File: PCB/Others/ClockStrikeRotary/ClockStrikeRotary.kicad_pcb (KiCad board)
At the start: 2 copper layers, 98 x 52 mm, 25 parts, among them J1 In, J2 Out, J3 Port 1, J4 Port 2, SW1 Rotary_Encoder_Switch

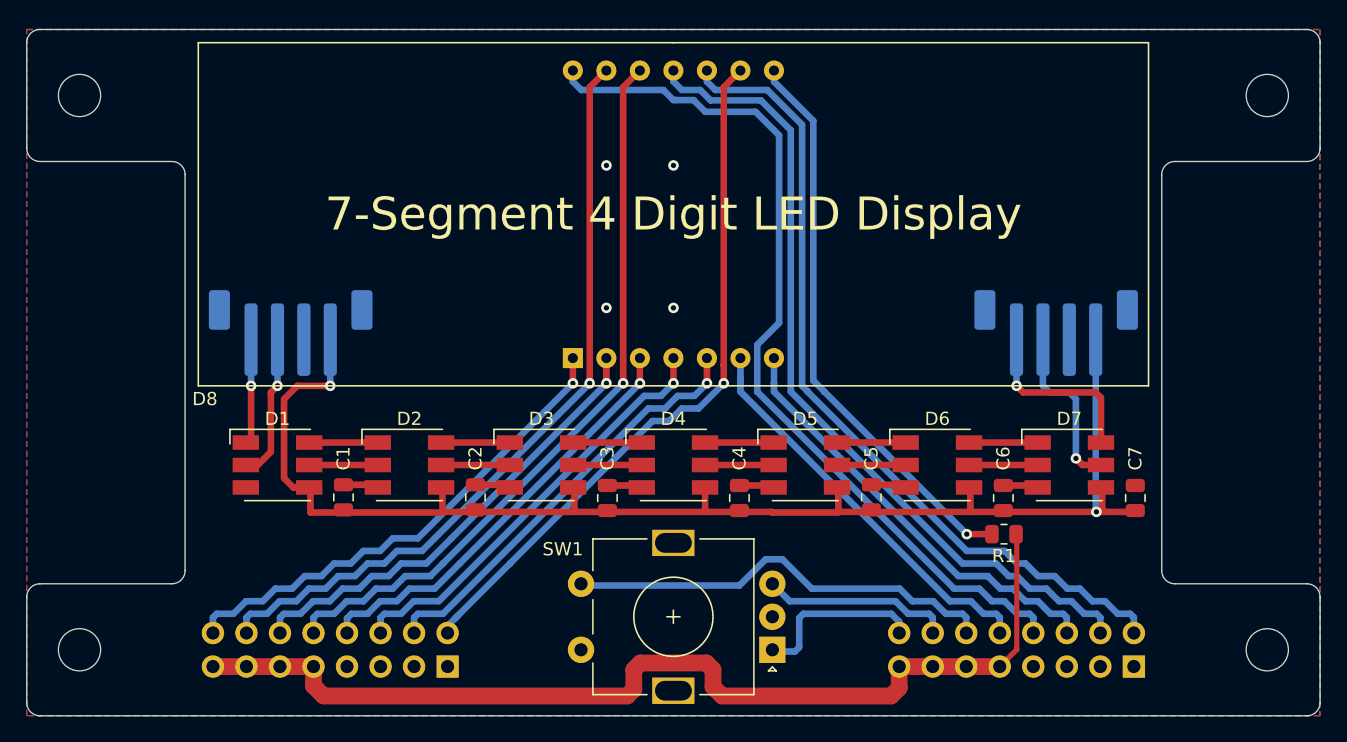
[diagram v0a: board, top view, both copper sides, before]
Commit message: Convert all KiCad to 6.0, clean up libraries, remove files that shouldn't be committed.
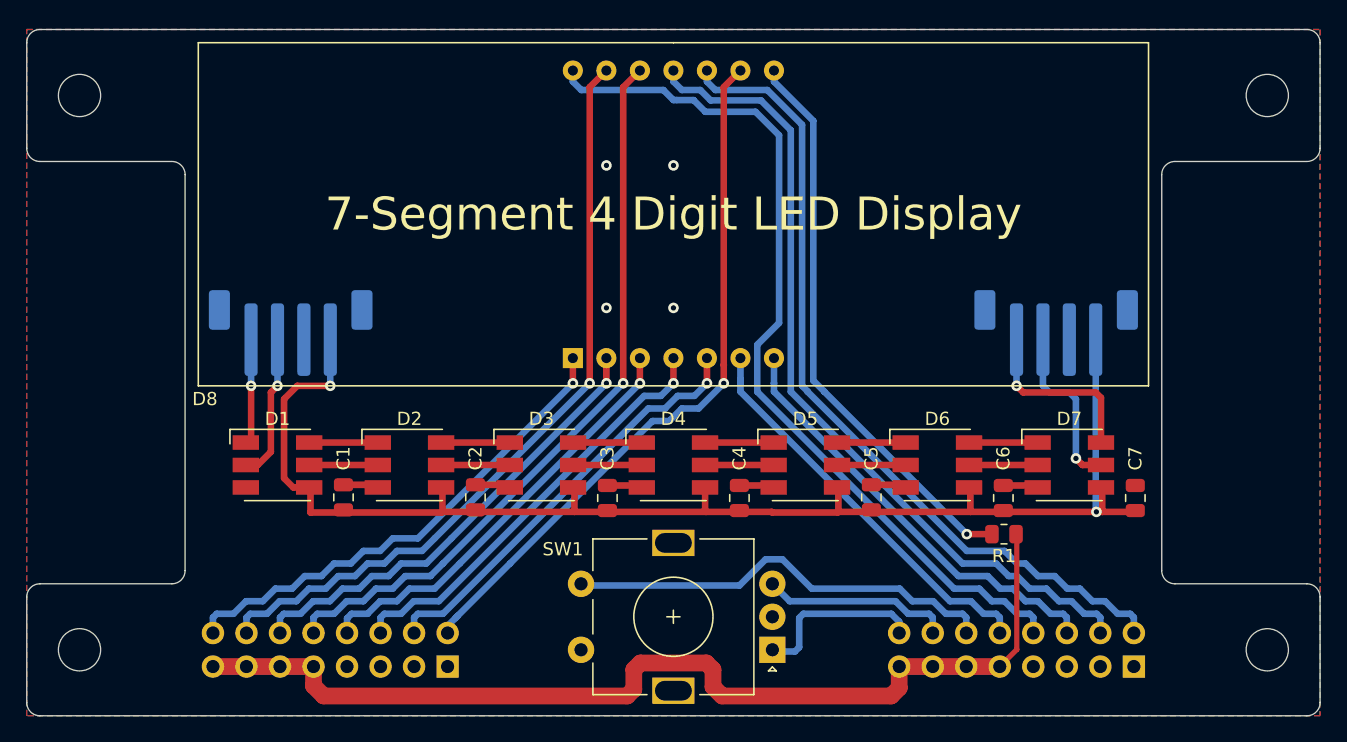
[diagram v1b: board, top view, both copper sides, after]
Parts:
- J3, J4: footprint Custom:PinHeader_2x08_P2.54mm_Vertical-Centered -> KTANE:PinHeader_2x08_P2.54mm_Vertical-Centered
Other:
- net class Default removed

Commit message: First pass of PCB rework.
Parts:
- removed J2: Out, Connector_JST:JST_PH_B4B-PH-SM4-TB_1x04-1MP_P2.00mm_Vertical
- removed REF** (x4): MountingHole_3.2mm_M3, MountingHole:MountingHole_3.2mm_M3
- added C10: 4.7nF, Capacitor_SMD:C_0603_1608Metric, B.Cu at (80.4, 66.3)
- added C11: 10uF, Capacitor_SMD:C_0603_1608Metric, B.Cu at (96.6, 41.2)
- added C12: 0.1μF, Capacitor_SMD:C_0603_1608Metric, B.Cu at (97.4, 38.9)
- added C8: 4.7nF, Capacitor_SMD:C_0603_1608Metric, B.Cu at (86.5, 66.3)
- added C9: 4.7nF, Capacitor_SMD:C_0603_1608Metric, B.Cu at (83.4, 66.3)
- added H1: MountingHole, MountingHole:MountingHole_3.2mm_M3, F.Cu at (20.0, 29.0)
- added H2: MountingHole, MountingHole:MountingHole_3.2mm_M3, F.Cu at (20.0, 71.0)
- added H3: MountingHole, MountingHole:MountingHole_3.2mm_M3, F.Cu at (110.0, 29.0)
- added H4: MountingHole, MountingHole:MountingHole_3.2mm_M3, F.Cu at (110.0, 71.0)
- added Q10: Q_NMOS_GSD, Package_TO_SOT_SMD:SOT-23, B.Cu at (64.5, 30.2)
- added Q11: Q_NMOS_GSD, Package_TO_SOT_SMD:SOT-23, B.Cu at (68.1, 30.2)
- added Q12: Q_NMOS_GSD, Package_TO_SOT_SMD:SOT-23, B.Cu at (71.2, 46.0)
- added Q9: Q_NMOS_GSD, Package_TO_SOT_SMD:SOT-23, B.Cu at (57.4, 30.2)
- added R18: 100, Resistor_SMD:R_0603_1608Metric, B.Cu at (58.1, 33.7)
- added R19: 10k, Resistor_SMD:R_0603_1608Metric, B.Cu at (56.6, 33.7)
- added R28: 10k, Resistor_SMD:R_0603_1608Metric, B.Cu at (63.9, 33.7)
- added R29: 100, Resistor_SMD:R_0603_1608Metric, B.Cu at (65.4, 33.7)
- added R30: 10k, Resistor_SMD:R_0603_1608Metric, B.Cu at (67.4, 33.7)
- added R31: 100, Resistor_SMD:R_0603_1608Metric, B.Cu at (68.9, 33.7)
- added R32: 10k, Resistor_SMD:R_0603_1608Metric, B.Cu at (74.7, 46.7)
- added R33: 100, Resistor_SMD:R_0603_1608Metric, B.Cu at (74.7, 45.2)
- added R36: 10k, Resistor_SMD:R_0603_1608Metric, B.Cu at (88.0, 66.3)
- added R37: 10k, Resistor_SMD:R_0603_1608Metric, B.Cu at (84.9, 66.3)
- added R38: 10k, Resistor_SMD:R_0603_1608Metric, B.Cu at (81.9, 66.3)
- added R39: 47k, Resistor_SMD:R_0603_1608Metric, B.Cu at (95.9, 38.9)
- added R40: 300, Resistor_SMD:R_0603_1608Metric, B.Cu at (59.9, 29.9)
- added R41: 300, Resistor_SMD:R_0603_1608Metric, B.Cu at (70.8, 29.9)
- added R42: 300, Resistor_SMD:R_0603_1608Metric, B.Cu at (65.0, 46.1)
- added R43: 300, Resistor_SMD:R_0603_1608Metric, B.Cu at (59.9, 46.1)
- added R44: 300, Resistor_SMD:R_0603_1608Metric, B.Cu at (57.4, 46.1)
- added R45: 300, Resistor_SMD:R_0603_1608Metric, B.Cu at (61.7, 29.9)
- added R46: 300, Resistor_SMD:R_0603_1608Metric, B.Cu at (67.5, 46.1)
- added R47: 300, Resistor_SMD:R_0603_1608Metric, B.Cu at (62.5, 46.1)
- added U1: PIC18F15Q40, Package_SO:SSOP-20_5.3x7.2mm_P0.65mm, B.Cu at (91.0, 36.2)
- C1, C2, C3, C4, C5, C6, C7: footprint Capacitor_SMD:C_0805_2012Metric -> Capacitor_SMD:C_0603_1608Metric
- J3: moved to F.Cu
- J4: value Port 2 -> ICSP; footprint KTANE:PinHeader_2x08_P2.54mm_Vertical-Centered -> Connector:Tag-Connect_TC2030-IDC-NL_2x03_P1.27mm_Vertical
- R1: footprint Resistor_SMD:R_0805_2012Metric -> Resistor_SMD:R_0603_1608Metric; moved to B.Cu
- moved J3 50.7 mm to (89.7, 71.0)
- moved J4 43.6 mm to (103.6, 29.2), turned to -90 degrees
- moved R1 36.8 mm to (72.6, 29.9), turned to 90 degrees
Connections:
- D7 pad 5: CO -> unconnected-(D7-CO-Pad5)
- D7 pad 6: DO -> unconnected-(D7-DO-Pad6)
- D8 pad 1: E -> Net-(D8-E)
- D8 pad 12: F -> Net-(D8-F)
- D8 pad 13: A -> Net-(D8-A)
- D8 pad 2: D -> Net-(D8-D)
- D8 pad 3: DP -> Net-(D8-DP)
- D8 pad 4: C -> Net-(D8-C)
- D8 pad 5: G -> Net-(D8-G)
- D8 pad 9: B -> Net-(D8-B)
- J3 pad 1: GND -> RE-B
- J3 pad 10: F -> ICSPCLK
- J3 pad 11: +5P -> unconnected-(J3-Pin_11-Pad11)
- J3 pad 12: D -> ICSPDAT
- J3 pad 13: +5P -> unconnected-(J3-Pin_13-Pad13)
- J3 pad 14: A -> SPI-CIPO
- J3 pad 15: +5P -> SPI-CS
- J3 pad 16: E -> GND
- J3 pad 2: B -> +5P
- J3 pad 3: GND -> RE-A
- J3 pad 4: G -> +3.3V
- J3 pad 5: GND -> RE-SW
- J3 pad 6: C -> I2C-CLK
- J3 pad 7: GND -> unconnected-(J3-Pin_7-Pad7)
- J3 pad 8: DP -> I2C-DAT
- J3 pad 9: +5P -> unconnected-(J3-Pin_9-Pad9)
- J4 pad 1: GND -> ~{MCLR}
- J4 pad 2: DIG3 -> +3.3V
- J4 pad 4: DIG2 -> ICSPDAT
- J4 pad 5: GND -> ICSPCLK
- J4 pad 6: COL -> unconnected-(J4-Pin_6-Pad6)
- R1 pad 1: +5P -> +3.3V
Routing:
- net +3.3V: track 0.00 -> 118.9 mm, vias 0 -> 6
- net +5P: track 77.6 -> 0.00 mm
- net DIG1: track 67.4 -> 2.19 mm
- net DIG2: track 62.8 -> 2.39 mm
- net DIG3: track 62.8 -> 2.40 mm
- net ICSPCLK: track 0.00 -> 54.6 mm, vias 0 -> 4
- net ICSPDAT: track 0.00 -> 49.4 mm, vias 0 -> 2
- net Net-(D8-COL): track 43.1 -> 1.92 mm, vias 1 -> 0
- net DIG-1: track 0.00 -> 40.4 mm, vias 0 -> 2
- net SPI-CS: track 0.00 -> 34.8 mm
- net DIG-2: track 0.00 -> 34.1 mm, vias 0 -> 2
- net DIG-3: track 0.00 -> 32.2 mm, vias 0 -> 2
- net B: track 53.5 -> 23.9 mm, vias 1 -> 0
- net DIG4: track 30.8 -> 3.00 mm
- net ~{MCLR}: track 0.00 -> 24.8 mm, vias 0 -> 2
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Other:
- board text added: "Keep Talking and Nobody Explodes - 4x7 Segment / Strikes / Encoder By Melair - Revision B01"
- board text removed: "Keep Talking and Nobody Explodes - 4x7 Segment / Strikes / Encoder By Melair - Revision A01"
- board text removed: "Port One"
- board text removed: "Port Two"
